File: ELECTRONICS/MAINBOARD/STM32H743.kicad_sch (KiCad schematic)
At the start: 28 parts, among them J10 Conn_01x05_Socket, J19 Conn_02x05_Odd_Even, SW1 RESET, SW2 BOOT, U19 STM32H743VITx, Y2 25mhz placeholder

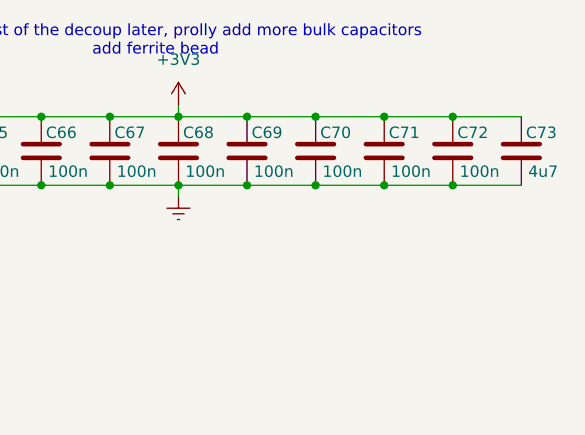
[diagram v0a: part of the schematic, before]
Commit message: decoup cap on h743
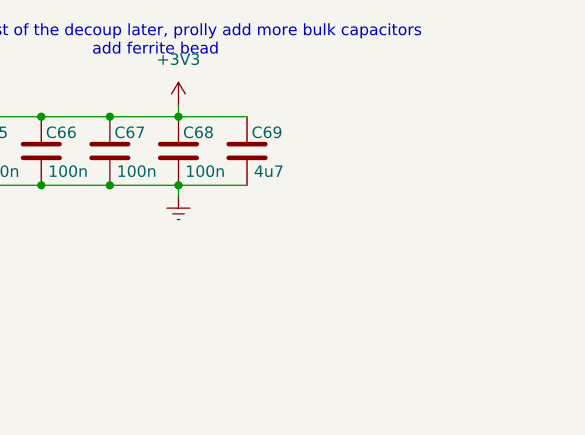
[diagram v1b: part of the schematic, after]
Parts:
- removed C69, C70, C71, C72: 100n, Capacitor_SMD:C_0402_1005Metric, symbol Device:C
- renumbered C73 to C69
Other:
- moved on the sheet: C69

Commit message: power zone
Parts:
- removed J10: Conn_01x05_Socket, Connector_PinHeader_2.54mm:PinHeader_1x05_P2.54mm_Vertical, symbol Connector:Conn_01x05_Socket
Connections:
- no-connect marks 5 -> 3
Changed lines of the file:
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@@
 		)
 	)
-	(text "SWIM NC\n"
-		(exclude_from_sim no)
-		(at 286.004 72.644 0)
-		(effects
-			(font
-				(size 1.27 1.27)
-			)
-		)
-	)
 	(text "\n THIS IS TEMPORARY PLACEMENT\n"
 		(exclude_from_sim no)
@@
 	)
 	(no_connect
-		(at 280.67 72.39)
-	)
-	(no_connect
 		(at 262.89 107.95)
 	)
@@
 		(at 250.19 100.33)
 	)
-	(no_connect
-		(at 280.67 80.01)
-	)
 	(wire
 		(pts
@@
 	(wire
 		(pts
-			(xy 280.67 69.85) (xy 292.1 69.85)
-		)
-		(stroke
-			(width 0)
-			(type default)
-		)
-	)
-	(wire
-		(pts
 			(xy 140.97 90.17) (xy 140.97 92.71)
 		)
@@
 	(wire
 		(pts
-			(xy 292.1 77.47) (xy 280.67 77.47)
-		)
-		(stroke
-			(width 0)
-			(type default)
-		)
-	)
-	(wire
-		(pts
 			(xy 250.19 97.79) (xy 238.76 97.79)
 		)
@@
 	(wire
 		(pts
-			(xy 280.67 74.93) (xy 295.91 74.93)
-		)
-		(stroke
-			(width 0)
-			(type default)
-		)
-	)
-	(wire
-		(pts
 			(xy 262.89 97.79) (xy 270.51 97.79)
 		)
@@
 		)
 	)
-	(label "3V3_SENSE"
-		(at 292.1 77.47 180)
-		(effects
-			(font
-				(size 1.27 1.27)
-			)
-			(justify right bottom)
-		)
-	)
 	(label "NRESET"
 		(at 238.76 97.79 0)
@@
 		)
 	)
-	(label "NRESET"
-		(at 292.1 69.85 180)
-		(effects
-			(font
-				(size 1.27 1.27)
-			)
-			(justify right bottom)
-		)
-	)
 	(label "SWDIO"
 		(at 224.79 120.65 180)
@@
 	(symbol
 		(lib_id "power:GNDREF")
-		(at 295.91 74.93 0)
-		(unit 1)
-		(body_style 1)
-		(exclude_from_sim no)
-		(in_bom yes)
-		(on_board yes)
-		(in_pos_files yes)
-		(dnp no)
-		(fields_autoplaced yes)
-		(property "Reference" "#PWR0100"
-			(at 295.91 81.28 0)
-			(hide yes)
-			(show_name no)
-			(do_not_autoplace no)
-			(effects
-				(font
-					(size 1.27 1.27)
-				)
-			)
-		)
-		(property "Value" "GNDREF"
-			(at 295.91 80.01 0)
-			(hide yes)
-			(show_name no)
-			(do_not_autoplace no)
-			(effects
-				(font
-					(size 1.27 1.27)
-				)
-			)
-		)
-		(property "Footprint" ""
-			(at 295.91 74.93 0)
-			(hide yes)
-			(show_name no)
-			(do_not_autoplace no)
-			(effects
-				(font
-					(size 1.27 1.27)
-				)
-			)
-		)
-		(property "Datasheet" ""
-			(at 295.91 74.93 0)
-			(hide yes)
-			(show_name no)
-			(do_not_autoplace no)
-			(effects
-				(font
-					(size 1.27 1.27)
-				)
-			)
-		)
-		(property "Description" "Power symbol creates a global label with name \"GNDREF\" , reference supply ground"
-			(at 295.91 74.93 0)
-			(hide yes)
-			(show_name no)
-			(do_not_autoplace no)
-			(effects
-				(font
-					(size 1.27 1.27)
-				)
-			)
-		)
-		(pin "1"
-		)
-		(instances
-			(project "autobot_mainboard"
-				(path "/f053f1d0-b1f5-4f80-9758-8ee1a2d3659d/81f4ef01-6699-40d7-b94c-738d9569ae26"
-					(reference "#PWR0100")
-					(unit 1)
-				)
-			)
-		)
-	)
-	(symbol
-		(lib_id "power:GNDREF")
 		(at 234.95 102.87 0)
 		(unit 1)
@@
 					(unit 1)
 				)
-			)
-		)
-	)
-	(symbol
-		(lib_id "Connector:Conn_01x05_Socket")
-		(at 275.59 74.93 180)
-		(unit 1)
-		(body_style 1)
-		(exclude_from_sim no)
-		(in_bom yes)
-		(on_board yes)
-		(in_pos_files yes)
-		(dnp no)
-		(property "Reference" "J10"
-			(at 276.606 63.754 0)
-			(show_name no)
-			(do_not_autoplace no)
-			(effects
-				(font
-					(size 1.27 1.27)
-				)
-			)
-		)
-		(property "Value" "Conn_01x05_Socket"
-			(at 276.606 66.294 0)
-			(show_name no)
-			(do_not_autoplace no)
-			(effects
-				(font
-					(size 1.27 1.27)
-				)
-			)
-		)
-		(property "Footprint" "Connector_PinHeader_2.54mm:PinHeader_1x05_P2.54mm_Vertical"
-			(at 275.59 74.93 0)
-			(hide yes)
-			(show_name no)
-			(do_not_autoplace no)
-			(effects
-				(font
-					(size 1.27 1.27)
-				)
-			)
-		)
-		(property "Datasheet" ""
-			(at 275.59 74.93 0)
-			(hide yes)
-			(show_name no)
-			(do_not_autoplace no)
-			(effects
-				(font
-					(size 1.27 1.27)
-				)
-			)
-		)
-		(property "Description" "Generic connector, single row, 01x05, script generated"
-			(at 275.59 74.93 0)
-			(hide yes)
-			(show_name no)
-			(do_not_autoplace no)
-			(effects
-				(font
-					(size 1.27 1.27)
-				)
-			)
-		)
-		(pin "3"
-		)
-		(pin "5"
-		)
-		(pin "4"
-		)
-		(pin "1"
-		)
-		(pin "2"
-		)
-		(instances
-			(project "autobot_mainboard"
-				(path "/f053f1d0-b1f5-4f80-9758-8ee1a2d3659d/81f4ef01-6699-40d7-b94c-738d9569ae26"
-					(reference "J10")
-					(unit 1)
-				)

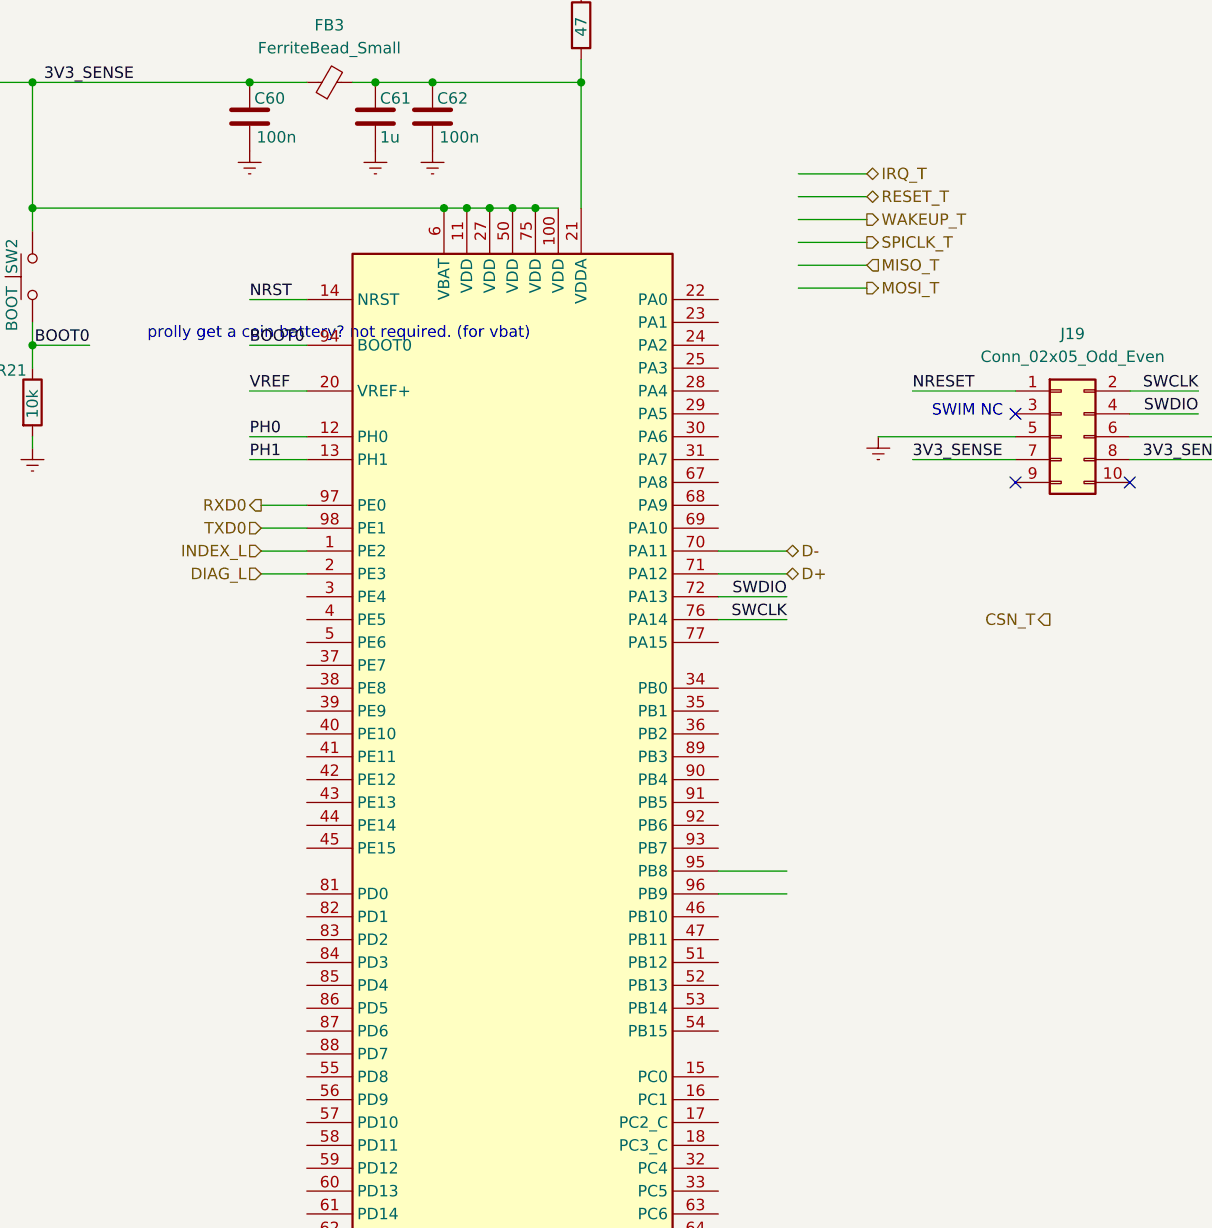
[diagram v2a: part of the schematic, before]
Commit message: change ToF module connection to use just one bus
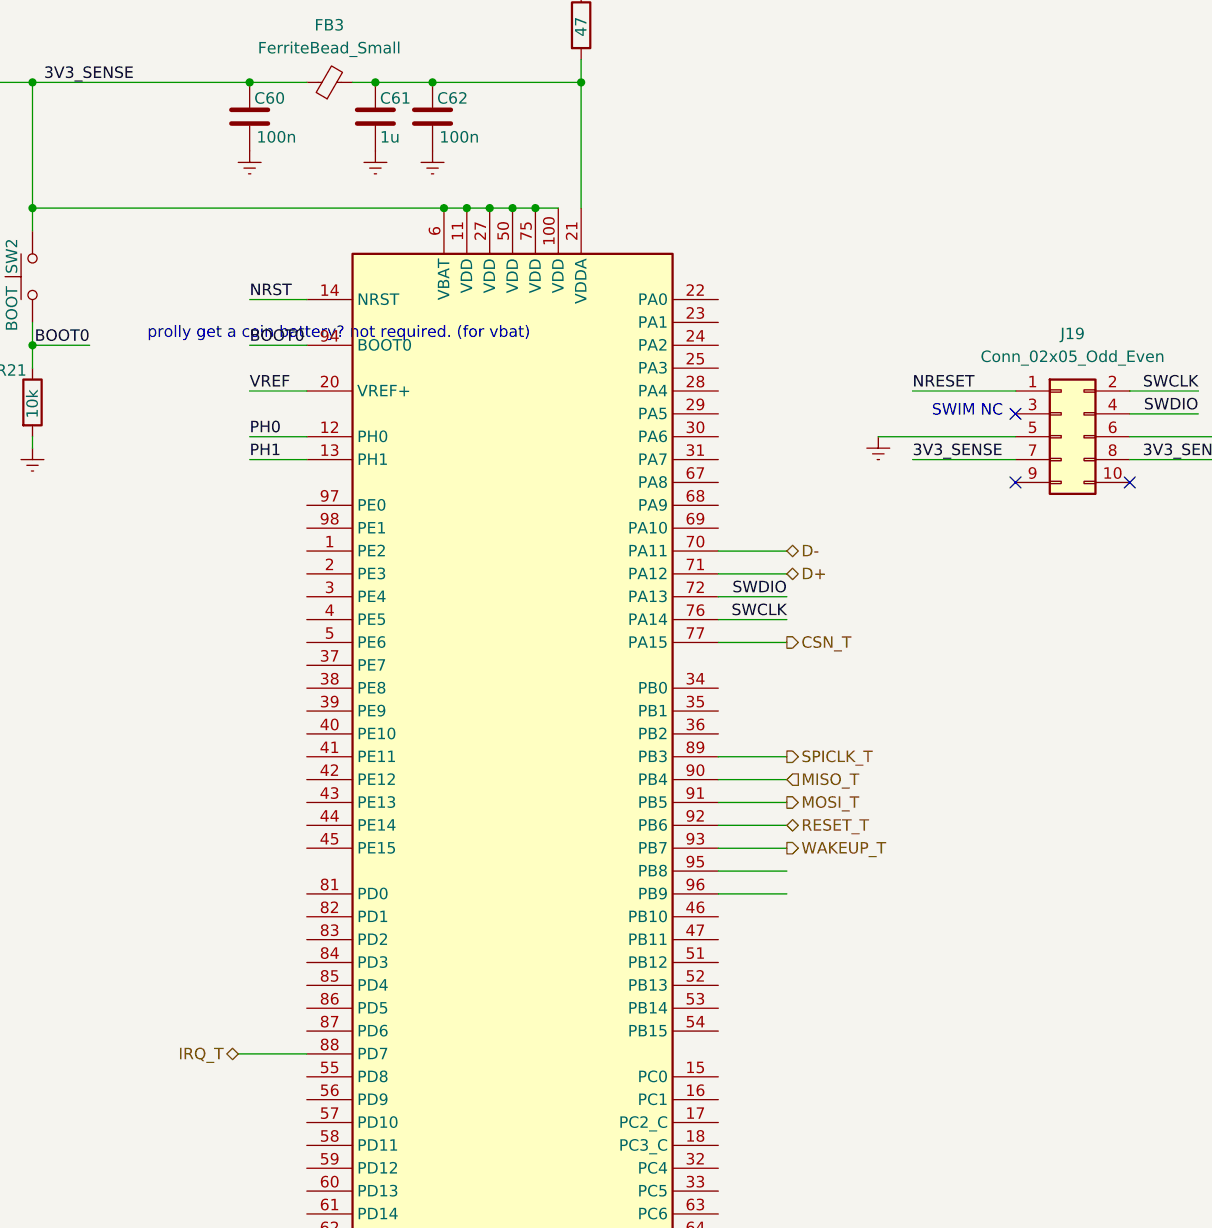
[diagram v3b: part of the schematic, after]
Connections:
- net CSN_T: now also U19.77 (PA15)
- net IRQ_T: now also U19.88 (PD7)
- net MISO_T: now also U19.90 (PB4)
- net MOSI_T: now also U19.91 (PB5)
- net RESET_T: now also U19.92 (PB6)
- net SPICLK_T: now also U19.89 (PB3)
- net WAKEUP_T: now also U19.93 (PB7)
- net DIAG_L: no longer names the net of U19.2 (PE3)
- net INDEX_L: no longer names the net of U19.1 (PE2)
- net RXD0: no longer names the net of U19.97 (PE0)
- net TXD0: no longer names the net of U19.98 (PE1)
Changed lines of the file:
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@@
-	(wire
-		(pts
-			(xy 226.06 78.74) (xy 233.68 78.74)
-		)
-		(stroke
-			(width 0)
-			(type default)
-		)
-	)
 	(wire
 		(pts
@@
 	(wire
 		(pts
+			(xy 217.17 146.05) (xy 224.79 146.05)
+		)
+		(stroke
+			(width 0)
+			(type default)
+		)
+	)
+	(wire
+		(pts
 			(xy 224.79 151.13) (xy 217.17 151.13)
 		)
@@
 	(wire
 		(pts
-			(xy 166.37 113.03) (xy 171.45 113.03)
+			(xy 217.17 138.43) (xy 224.79 138.43)
 		)
 		(stroke
@@
 	(wire
 		(pts
+			(xy 217.17 148.59) (xy 224.79 148.59)
+		)
+		(stroke
+			(width 0)
+			(type default)
+		)
+	)
+	(wire
+		(pts
 			(xy 279.4 43.18) (xy 287.02 43.18)
 		)
@@
 	(wire
 		(pts
-			(xy 166.37 110.49) (xy 171.45 110.49)
-		)
-		(stroke
-			(width 0)
-			(type default)
-		)
-	)
-	(wire
-		(pts
 			(xy 186.69 77.47) (xy 189.23 77.47)
 		)
@@
 	(wire
 		(pts
-			(xy 226.06 76.2) (xy 233.68 76.2)
-		)
-		(stroke
-			(width 0)
-			(type default)
-		)
-	)
-	(wire
-		(pts
 			(xy 201.93 63.5) (xy 201.93 77.47)
 		)
@@
 	(wire
 		(pts
-			(xy 166.37 115.57) (xy 171.45 115.57)
-		)
-		(stroke
-			(width 0)
-			(type default)
-		)
-	)
-	(wire
-		(pts
 			(xy 194.31 77.47) (xy 196.85 77.47)
 		)
@@
 	(wire
 		(pts
-			(xy 226.06 83.82) (xy 233.68 83.82)
-		)
-		(stroke
-			(width 0)
-			(type default)
-		)
-	)
-	(wire
-		(pts
-			(xy 166.37 118.11) (xy 171.45 118.11)
-		)
-		(stroke
-			(width 0)
-			(type default)
-		)
-	)
-	(wire
-		(pts
 			(xy 302.26 50.8) (xy 309.88 50.8)
 		)
@@
 	(wire
 		(pts
+			(xy 224.79 140.97) (xy 217.17 140.97)
+		)
+		(stroke
+			(width 0)
+			(type default)
+		)
+	)
+	(wire
+		(pts
 			(xy 140.97 102.87) (xy 140.97 104.14)
 		)
@@
 	(wire
 		(pts
-			(xy 226.06 73.66) (xy 233.68 73.66)
+			(xy 171.45 171.45) (xy 163.83 171.45)
 		)
 		(stroke
@@
 	(wire
 		(pts
-			(xy 226.06 86.36) (xy 233.68 86.36)
+			(xy 217.17 143.51) (xy 224.79 143.51)
 		)
 		(stroke
@@
 	(wire
 		(pts
-			(xy 226.06 81.28) (xy 233.68 81.28)
-		)
-		(stroke
-			(width 0)
-			(type default)
-		)
-	)
-	(wire
-		(pts
 			(xy 165.1 97.79) (xy 171.45 97.79)
 		)
@@
 		(pts
 			(xy 194.31 222.25) (xy 195.58 222.25)
+		)
+		(stroke
+			(width 0)
+			(type default)
+		)
+	)
+	(wire
+		(pts
+			(xy 224.79 125.73) (xy 217.17 125.73)
 		)
 		(stroke
@@
 	(hierarchical_label "CSN_T"
 		(shape output)
-		(at 254 123.19 180)
+		(at 224.79 125.73 0)
+		(effects
+			(font
+				(size 1.27 1.27)
+			)
+			(justify left)
+		)
+	)
+	(hierarchical_label "VL_XSHUT_2"
+		(shape output)
+		(at 102.87 187.96 0)
+		(effects
+			(font
+				(size 1.27 1.27)
+			)
+			(justify left)
+		)
+	)
+	(hierarchical_label "BMI_MOSI_L"
+		(shape output)
+		(at 119.38 151.13 0)
+		(effects
+			(font
+				(size 1.27 1.27)
+			)
+			(justify left)
+		)
+	)
+	(hierarchical_label "SPICLK_B"
+		(shape output)
+		(at 104.14 132.08 180)
 		(effects
 			(font
@@
 		)
 	)
-	(hierarchical_label "VL_XSHUT_2"
-		(shape output)
-		(at 102.87 187.96 0)
-		(effects
-			(font
-				(size 1.27 1.27)
-			)
-			(justify left)
-		)
-	)
-	(hierarchical_label "RXD0"
-		(shape output)
-		(at 166.37 110.49 180)
-		(effects
-			(font
-				(size 1.27 1.27)
-			)
-			(justify right)
-		)
-	)
-	(hierarchical_label "BMI_MOSI_L"
-		(shape output)
-		(at 119.38 151.13 0)
-		(effects
-			(font
-				(size 1.27 1.27)
-			)
-			(justify left)
-		)
-	)
-	(hierarchical_label "SPICLK_B"
-		(shape output)
-		(at 104.14 132.08 180)
-		(effects
-			(font
-				(size 1.27 1.27)
-			)
-			(justify right)
-		)
-	)
-	(hierarchical_label "INDEX_L"
-		(shape input)
-		(at 166.37 115.57 180)
-		(effects
-			(font
-				(size 1.27 1.27)
-			)
-			(justify right)
-		)
-	)
 	(hierarchical_label "BMI_SCK_R"
 		(shape bidirectional)
@@
 	(hierarchical_label "WAKEUP_T"
 		(shape output)
-		(at 233.68 78.74 0)
+		(at 224.79 148.59 0)
 		(effects
 			(font
@@
 	(hierarchical_label "MOSI_T"
 		(shape output)
-		(at 233.68 86.36 0)
+		(at 224.79 143.51 0)
 		(effects
 			(font
@@
 			)
 			(justify left)
-		)
-	)
-	(hierarchical_label "DIAG_L"
-		(shape input)
-		(at 166.37 118.11 180)
-		(effects
-			(font
-				(size 1.27 1.27)
-			)
-			(justify right)
 		)
 	)
 	(hierarchical_label "MISO_T"
 		(shape input)
-		(at 233.68 83.82 0)
+		(at 224.79 140.97 0)
 		(effects
 			(font
@@
 	(hierarchical_label "SPICLK_T"
 		(shape output)
-		(at 233.68 81.28 0)
+		(at 224.79 138.43 0)
 		(effects
 			(font
@@
 	(hierarchical_label "RESET_T"
 		(shape bidirectional)
-		(at 233.68 76.2 0)
+		(at 224.79 146.05 0)
 		(effects
 			(font
@@
 		)
 	)
-	(hierarchical_label "TXD0"
-		(shape input)
-		(at 166.37 113.03 180)
+	(hierarchical_label "RESET_B"
+		(shape bidirectional)
+		(at 104.14 129.54 180)
 		(effects
 			(font
@@
 		)
 	)
-	(hierarchical_label "RESET_B"
-		(shape bidirectional)
-		(at 104.14 129.54 180)
+	(hierarchical_label "IRQ_T"
+		(shape bidirectional)
+		(at 163.83 171.45 180)
 		(effects
 			(font
@@
 		)
 	)
-	(hierarchical_label "IRQ_T"
-		(shape bidirectional)
-		(at 233.68 73.66 0)
-		(effects
-			(font
-				(size 1.27 1.27)
-			)
-			(justify left)
-		)
-	)

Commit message: 10/24 save
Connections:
- net BMI_CS_R: now also U19.41 (PE11)
- net BMI_MISO_R: now also U19.43 (PE13)
- net BMI_MOSI_R: now also U19.44 (PE14)
- net BMI_SCK_R: now also U19.42 (PE12)
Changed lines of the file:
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@@
-		)
-	)
-	(hierarchical_label "VL_SCL_3"
-		(shape bidirectional)
-		(at 119.38 180.34 0)
-		(effects
-			(font
-				(size 1.27 1.27)
-			)
-			(justify left)
 		)
 	)
@@
 		)
 	)
-	(hierarchical_label "VL_SDA_2"
-		(shape bidirectional)
-		(at 102.87 182.88 0)
-		(effects
-			(font
-				(size 1.27 1.27)
-			)
-			(justify left)
-		)
-	)
 	(hierarchical_label "MOSI_B"
 		(shape output)
@@
 		)
 	)
-	(hierarchical_label "VL_SCL_2"
-		(shape bidirectional)
-		(at 102.87 180.34 0)
-		(effects
-			(font
-				(size 1.27 1.27)
-			)
-			(justify left)
-		)
-	)
 	(hierarchical_label "3V3"
 		(shape input)
@@
 	(hierarchical_label "BMI_SCK_R"
 		(shape bidirectional)
-		(at 102.87 153.67 0)
-		(effects
-			(font
-				(size 1.27 1.27)
-			)
-			(justify left)
+		(at 171.45 140.97 180)
+		(effects
+			(font
+				(size 1.27 1.27)
+			)
+			(justify right)
 		)
 	)
@@
 		)
 	)
-	(hierarchical_label "VL_SDA_1"
-		(shape bidirectional)
-		(at 119.38 168.91 0)
-		(effects
-			(font
-				(size 1.27 1.27)
-			)
-			(justify left)
-		)
-	)
 	(hierarchical_label "VL_IO_3"
 		(shape bidirectional)
@@
 	(hierarchical_label "BMI_MISO_R"
 		(shape input)
-		(at 102.87 160.02 0)
-		(effects
-			(font
-				(size 1.27 1.27)
-			)
-			(justify left)
+		(at 171.45 143.51 180)
+		(effects
+			(font
+				(size 1.27 1.27)
+			)
+			(justify right)
 		)
 	)
 	(hierarchical_label "BMI_CS_R"
 		(shape bidirectional)
-		(at 102.87 156.21 0)
-		(effects
-			(font
-				(size 1.27 1.27)
-			)
-			(justify left)
+		(at 171.45 138.43 180)
+		(effects
+			(font
+				(size 1.27 1.27)
+			)
+			(justify right)
 		)
 	)
@@
 		)
 	)
-	(hierarchical_label "VL_SCL_1"
-		(shape bidirectional)
-		(at 119.38 166.37 0)
-		(effects
-			(font
-				(size 1.27 1.27)
-			)
-			(justify left)
-		)
-	)
 	(hierarchical_label "VL_SCL_0"
 		(shape bidirectional)
@@
 	(hierarchical_label "BMI_MOSI_R"
 		(shape output)
-		(at 102.87 151.13 0)
-		(effects
-			(font
-				(size 1.27 1.27)
-			)
-			(justify left)
+		(at 171.45 146.05 180)
+		(effects
+			(font
+				(size 1.27 1.27)
+			)
+			(justify right)
 		)
 	)
@@
 	(hierarchical_label "BMI_INT_R"
 		(shape output)
-		(at 102.87 146.05 0)
+		(at 151.13 137.16 0)
 		(effects
 			(font
@@
 		(effects
 			(font
-				(size 1.27 1.27)
-			)
-			(justify left)
-		)
-	)
-	(hierarchical_label "VL_SDA_3"
-		(shape bidirectional)
-		(at 119.38 182.88 0)
-		(effects
-			(font
